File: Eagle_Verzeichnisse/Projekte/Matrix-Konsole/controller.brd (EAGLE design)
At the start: 114.3 x 63.2 mm, 21 parts, among them IC1 74HC165D

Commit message: Improved layouts
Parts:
- moved C3 14.5 mm to (57.1, 8.89)
- moved C5 14.5 mm to (52.1, 38.1)
- moved R5 14.5 mm to (52.1, 26.7)
- moved BUT2 14.5 mm to (23.0, 47.7)
- moved BUT3 14.5 mm to (8.03, 32.7)
- moved BUT4 14.5 mm to (38.0, 32.7)
- moved BUT5 14.5 mm to (103.0, 42.7)
- moved C1 14.5 mm to (59.7, 41.9)
- moved C2 14.5 mm to (63.5, 57.1)
- moved C6 14.5 mm to (85.1, 57.1)
- moved C7 14.5 mm to (77.5, 57.1)
- moved IC1 14.5 mm to (68.6, 31.8)
- moved R2 14.5 mm to (49.5, 57.1)
- moved R3 14.5 mm to (80.0, 40.6)
- moved BUT1 14.5 mm to (23.0, 17.7)
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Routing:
- net GND: track 324.3 -> 337.7 mm
- net D0: track 200.8 -> 199.0 mm

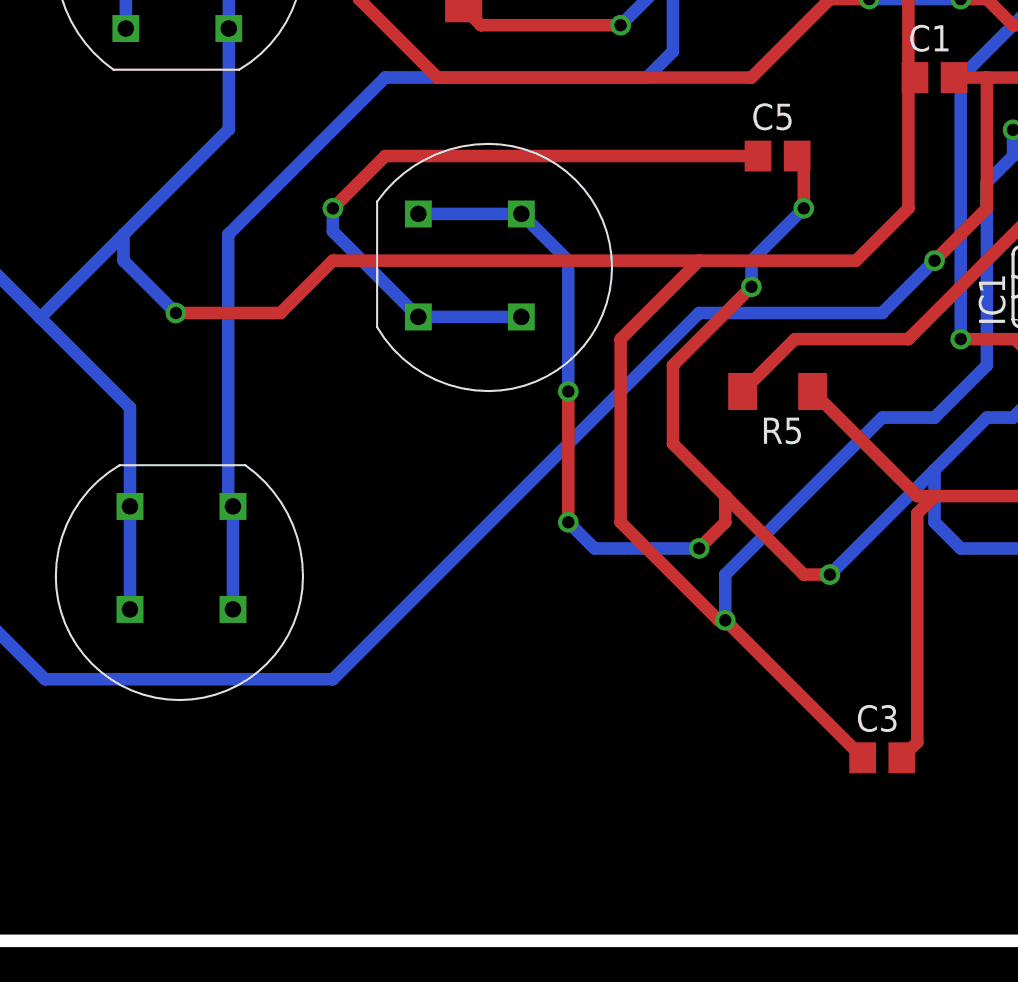
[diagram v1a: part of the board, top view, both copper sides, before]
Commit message: Splitted the console-layout into three boards and improved the layouts
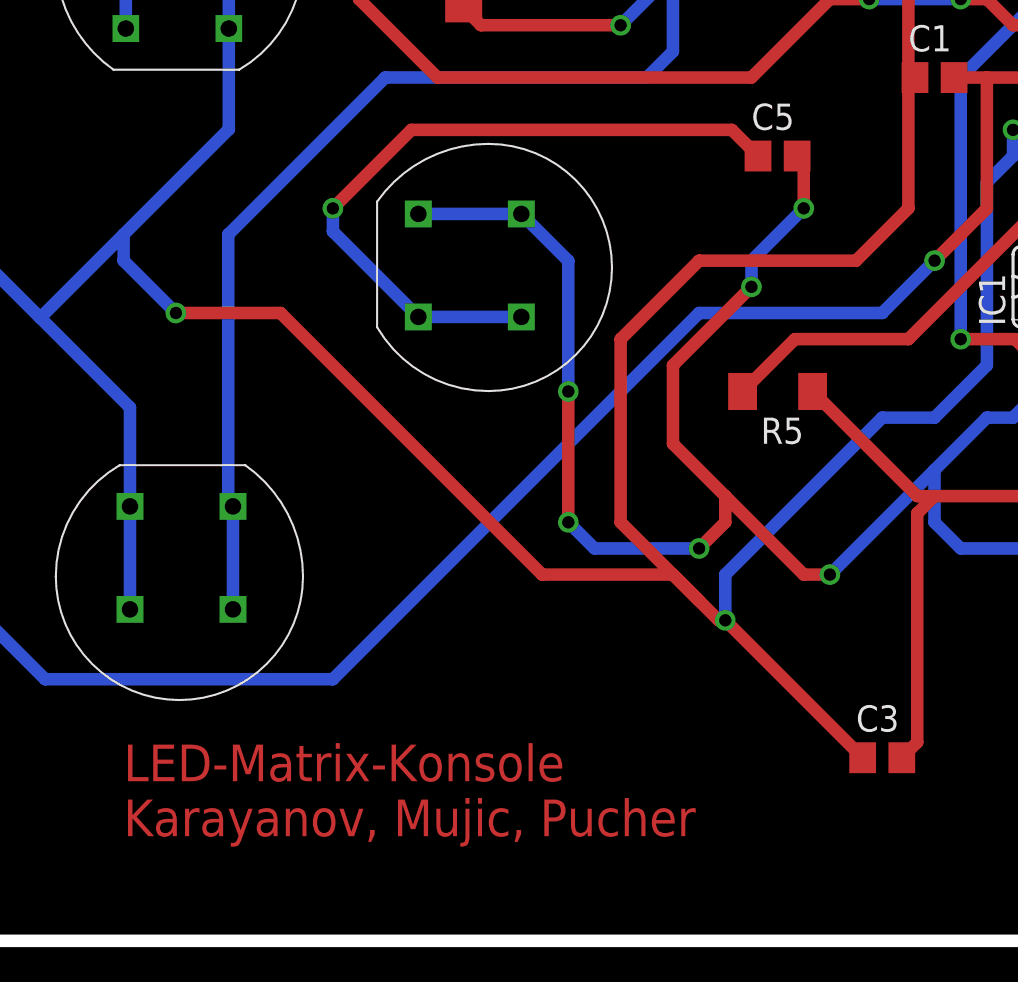
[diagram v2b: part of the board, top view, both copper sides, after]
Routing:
- net GND: track 337.7 -> 342.4 mm
- net N3: track 33.7 -> 34.7 mm
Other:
- board text added: "LED-Matrix-Konsole Karayanov, Mujic, Pucher"
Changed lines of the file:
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@@
 <?xml version="1.0" encoding="utf-8"?>
 <!DOCTYPE eagle SYSTEM "eagle.dtd">
-<eagle version="8.1.0">
+<eagle version="8.0.2">
 <drawing>
 <settings>
@@
 <wire x1="114.28" y1="63.17" x2="0" y2="63.17" width="0.6096" layer="20"/>
 <wire x1="0" y1="63.17" x2="0" y2="0" width="0.6096" layer="20"/>
+<text x="20.32" y="5.08" size="1.778" layer="1">LED-Matrix-Konsole
+Karayanov, Mujic, Pucher</text>
 </plain>
 <attributes>
@@
 <via x="22.86" y="30.48" extent="1-16" drill="0.6"/>
 <wire x1="22.86" y1="30.48" x2="27.94" y2="30.48" width="0.6096" layer="1"/>
-<wire x1="27.94" y1="30.48" x2="30.48" y2="33.02" width="0.6096" layer="1"/>
-<wire x1="48.26" y1="33.02" x2="30.48" y2="33.02" width="0.6096" layer="1"/>
 <wire x1="48.26" y1="33.02" x2="55.88" y2="33.02" width="0.6096" layer="1"/>
 <wire x1="55.88" y1="33.02" x2="58.42" y2="35.56" width="0.6096" layer="1"/>
@@
 <via x="49.53" y="15.56" extent="1-16" drill="0.6"/>
 <wire x1="49.21" y1="15.56" x2="49.53" y2="15.56" width="0.6096" layer="1"/>
-<wire x1="44.45" y1="20.32" x2="49.21" y2="15.56" width="0.6096" layer="1"/>
+<wire x1="48.26" y1="16.51" x2="44.45" y2="20.32" width="0.6096" layer="1"/>
+<wire x1="48.26" y1="16.51" x2="49.21" y2="15.56" width="0.6096" layer="1"/>
 <wire x1="62.23" y1="36.83" x2="62.23" y2="27.94" width="0.6096" layer="16"/>
 <wire x1="59.69" y1="25.4" x2="57.15" y2="25.4" width="0.6096" layer="16"/>
@@
 <wire x1="106.426" y1="48.641" x2="107.569" y2="48.641" width="0.6096" layer="1"/>
 <wire x1="107.569" y1="48.641" x2="110.49" y2="45.72" width="0.6096" layer="1"/>
+<wire x1="40.64" y1="17.78" x2="46.99" y2="17.78" width="0.6096" layer="1"/>
+<wire x1="46.99" y1="17.78" x2="48.26" y2="16.51" width="0.6096" layer="1"/>
+<wire x1="27.94" y1="30.48" x2="40.64" y2="17.78" width="0.6096" layer="1"/>
 </signal>
 <signal name="D0">
@@
 <contactref element="C5" pad="1"/>
 <wire x1="34.63" y1="30.29" x2="39.63" y2="30.29" width="0.6096" layer="16"/>
-<wire x1="51.12" y1="38.1" x2="33.02" y2="38.1" width="0.6096" layer="1"/>
-<wire x1="33.02" y1="38.1" x2="30.48" y2="35.56" width="0.6096" layer="1"/>
 <via x="30.48" y="35.56" extent="1-16" drill="0.6"/>
 <wire x1="30.48" y1="35.56" x2="30.48" y2="34.44" width="0.6096" layer="16"/>
 <wire x1="30.48" y1="34.44" x2="34.63" y2="30.29" width="0.6096" layer="16"/>
+<wire x1="34.29" y1="39.37" x2="49.85" y2="39.37" width="0.6096" layer="1"/>
+<wire x1="49.85" y1="39.37" x2="51.12" y2="38.1" width="0.6096" layer="1"/>
+<wire x1="30.48" y1="35.56" x2="34.29" y2="39.37" width="0.6096" layer="1"/>
 </signal>
 <signal name="5V">
@@
 </board>
 </drawing>
+<compatibility>
+<note version="6.3" minversion="6.2.2" severity="warning">
+Since Version 6.2.2 text objects can contain more than one line,
+which will not be processed correctly with this version.
+</note>
+</compatibility>
 </eagle>

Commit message: Made final changes to the layout and added PDF-Files
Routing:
- net N$8: track 0.00 -> 355.6 mm
- net D1: track 120.1 -> 126.6 mm
- net GND: track 342.4 -> 336.8 mm
- net D5: track 71.3 -> 75.3 mm
- net D3: track 136.0 -> 134.4 mm
- net D4: track 81.9 -> 83.4 mm
- net N$2: track 40.8 -> 42.3 mm
- net N$3: track 19.8 -> 21.3 mm
- net D0: track 199.0 -> 198.2 mm
- net 5V: track 183.0 -> 182.4 mm
- net D2: track 112.1 -> 112.6 mm
